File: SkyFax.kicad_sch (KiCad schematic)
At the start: 16 parts, among them J1 RJ11/12, J4 Conn_02x08_Odd_Even, J5 Conn_01x02, J6 Conn_01x02

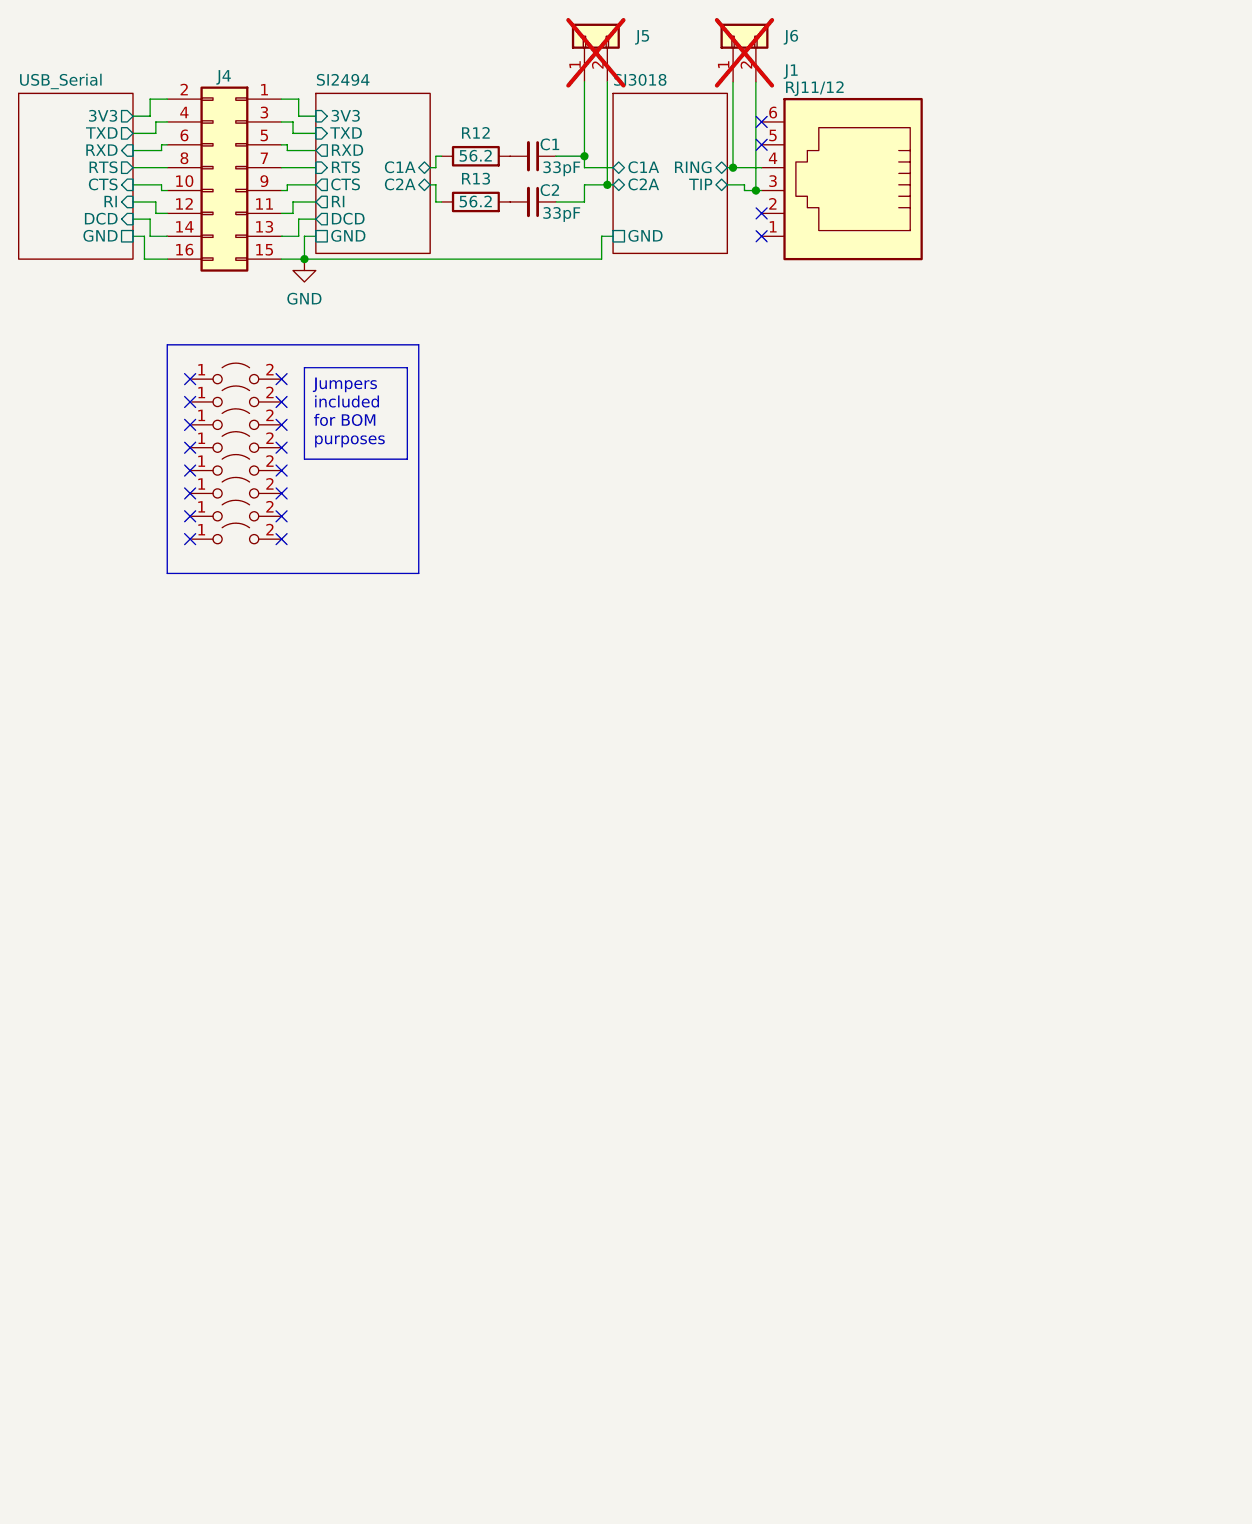
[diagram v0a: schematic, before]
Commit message: [4.0] M.2 Module. Sent to fab
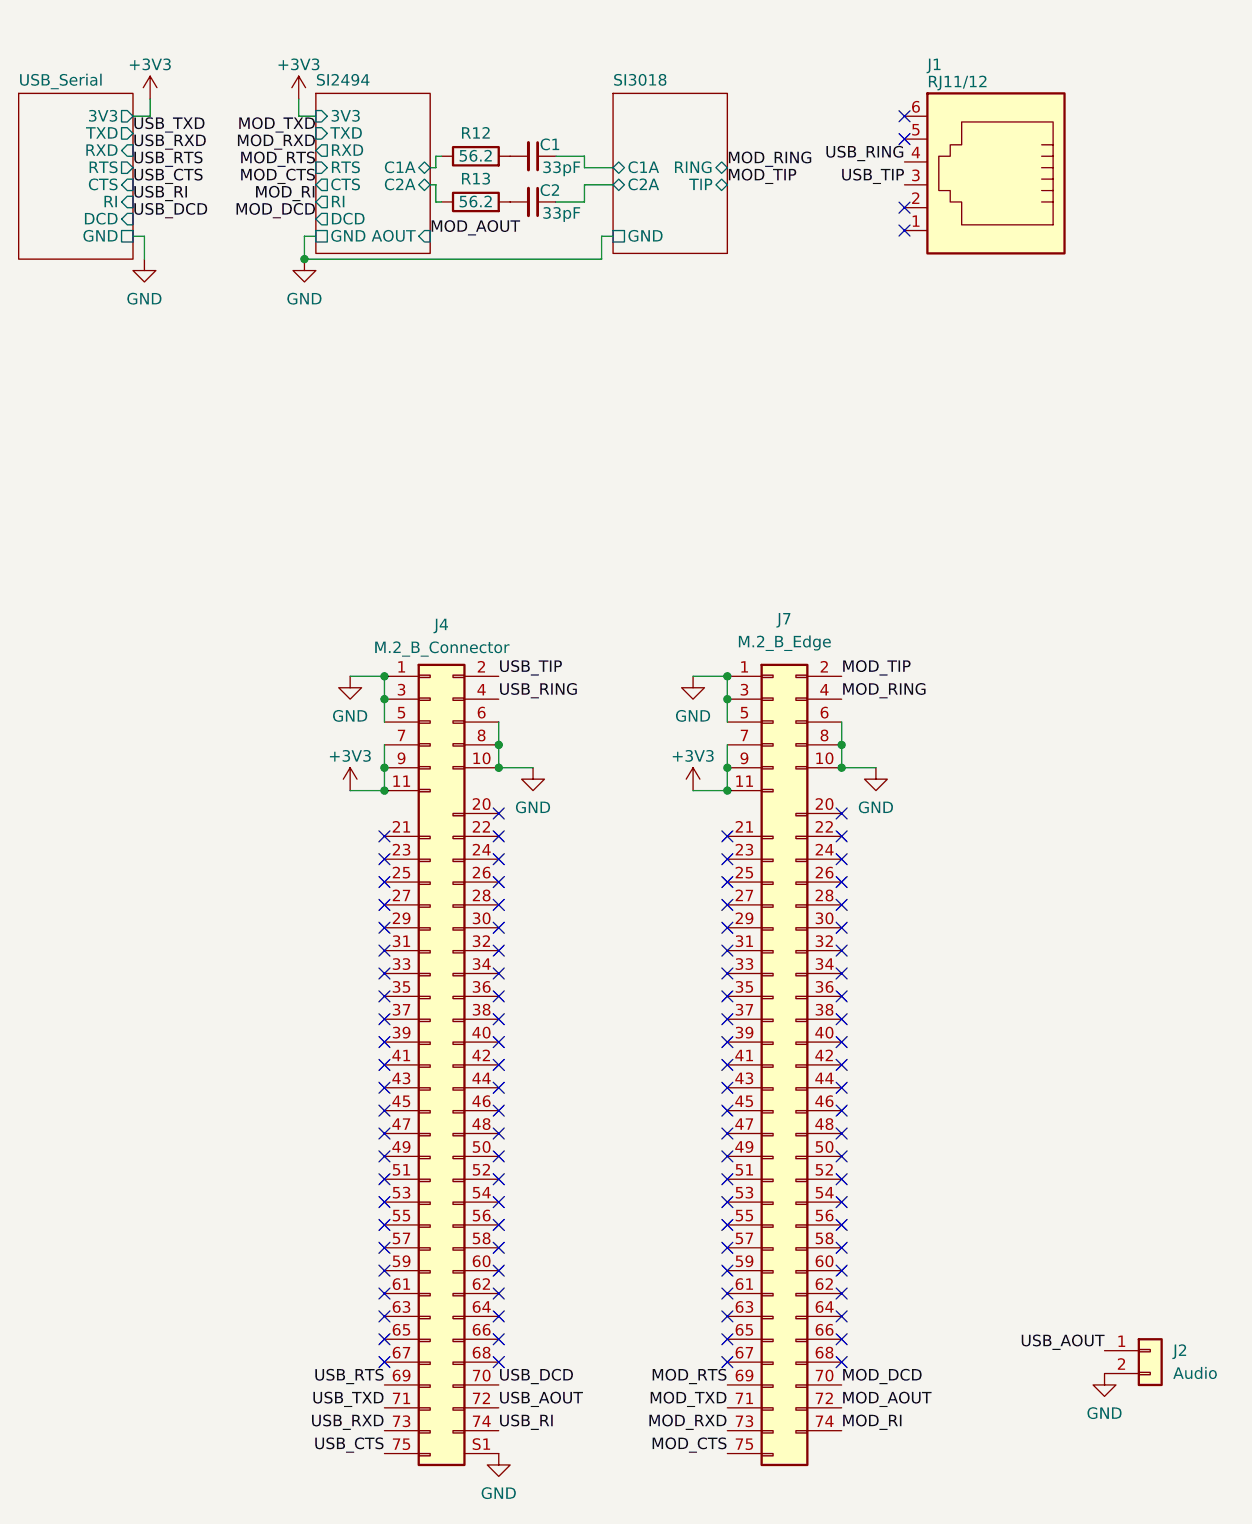
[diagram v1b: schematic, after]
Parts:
- removed J4: Conn_02x08_Odd_Even, Connector_PinHeader_2.54mm:PinHeader_2x08_P2.54mm_Vertical, symbol Connector_Generic:Conn_02x08_Odd_Even
- removed J5, J6: Conn_01x02, Connector_PinSocket_2.54mm:PinSocket_1x02_P2.54mm_Vertical, symbol Connector_Generic:Conn_01x02
- removed JP1, JP2, JP3, JP4, JP5, JP6, JP7, JP8: Jumper_2_Open, symbol Jumper:Jumper_2_Open
- added J2: Audio, Connector_PinSocket_2.54mm:PinSocket_1x02_P2.54mm_Vertical, symbol Connector_Generic:Conn_01x02
- added J4: M.2_B_Connector, SkyFax:AMPHENOL_MDT420B01001_2260, symbol SkyFax:M.2_B_Connector
- added J7: M.2_B_Edge, SkyFax:M.2-B-KEY_2260, symbol SkyFax:M.2_B_Edge
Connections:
- net GND: now also J2.2 (Pin_2), J4.1 (Pin_1), J4.10 (Pin_10), J4.3 (Pin_3), J4.5 (Pin_5), J4.6 (Pin_6), J4.8 (Pin_8), J4.S1 (SHIELD), J4.S2 (SHIELD), J7.1 (Pin_1), J7.10 (Pin_10), J7.3 (Pin_3), J7.5 (Pin_5), J7.6 (Pin_6), J7.8 (Pin_8)
- net SI3018/RING renamed USB_RING
- net USB_RING: now also J4.4 (Pin_4)
- net SI3018/TIP renamed USB_TIP
- net USB_TIP: now also J4.2 (Pin_2)
- new net +3V3: J4.11 (Pin_11), J4.7 (Pin_7), J4.9 (Pin_9), J7.11 (Pin_11), J7.7 (Pin_7), J7.9 (Pin_9)
- new net MOD_AOUT: J7.72 (Pin_72)
- new net MOD_CTS: J7.75 (Pin_75)
- new net MOD_DCD: J7.70 (Pin_70)
- new net MOD_RI: J7.74 (Pin_74)
- new net MOD_RING: J7.4 (Pin_4)
- new net MOD_RTS: J7.69 (Pin_69)
- new net MOD_RXD: J7.73 (Pin_73)
- new net MOD_TIP: J7.2 (Pin_2)
- new net MOD_TXD: J7.71 (Pin_71)
- new net USB_AOUT: J2.1 (Pin_1), J4.72 (Pin_72)
- new net USB_CTS: J4.75 (Pin_75)
- new net USB_DCD: J4.70 (Pin_70)
- new net USB_RI: J4.74 (Pin_74)
- new net USB_RTS: J4.69 (Pin_69)
- new net USB_RXD: J4.73 (Pin_73)
- new net USB_TXD: J4.71 (Pin_71)
- no-connect marks 20 -> 102
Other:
- sheet SI2494 ports: added AOUT; removed none
- moved on the sheet: J1

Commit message: [4.2] Sound card
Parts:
- J2: footprint Connector_PinSocket_2.54mm:PinSocket_1x02_P2.54mm_Vertical -> Connector_PinSocket_2.54mm:PinSocket_1x03_P2.54mm_Vertical; symbol Connector_Generic:Conn_01x02 -> Connector_Generic:Conn_01x03
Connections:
- net +3V3: now also J2.3 (Pin_3)
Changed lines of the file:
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@@
     (title "SkyFax")
     (date "2023-09-12")
-    (rev "4.0")
+    (rev "4.1")
     (company "Brian Hong")
     (comment 1 "@im_eningeer")
@@
     (stroke (width 0) (type default))
   )
+  (wire (pts (xy 139.7 173.99) (xy 137.795 173.99))
+    (stroke (width 0) (type default))
+  )
   (wire (pts (xy 59.69 96.52) (xy 55.88 96.52))
     (stroke (width 0) (type default))
@@
     (stroke (width 0) (type default))
   )
+  (wire (pts (xy 137.795 173.99) (xy 137.795 178.435))
+    (stroke (width 0) (type default))
+  )
   (wire (pts (xy 65.405 40.005) (xy 65.405 38.735))
     (stroke (width 0) (type default))
@@
   )
   (wire (pts (xy 110.49 101.6) (xy 110.49 104.14))
+    (stroke (width 0) (type default))
+  )
+  (wire (pts (xy 139.7 176.53) (xy 129.54 176.53))
+    (stroke (width 0) (type default))
+  )
+  (wire (pts (xy 129.54 168.91) (xy 129.54 176.53))
     (stroke (width 0) (type default))
   )
@@
     )
   )
-  (symbol (lib_id "power:GND") (at 139.7 173.99 0) (mirror y) (unit 1)
+  (symbol (lib_id "power:GND") (at 137.795 178.435 0) (mirror y) (unit 1)
     (in_bom yes) (on_board yes) (dnp no) (fields_autoplaced)
-    (property "Reference" "#PWR045" (at 139.7 180.34 0)
-      (effects (font (size 1.27 1.27)) hide)
-    )
-    (property "Value" "GND" (at 139.7 178.435 0)
-      (effects (font (size 1.27 1.27)))
-    )
-    (property "Footprint" "" (at 139.7 173.99 0)
-      (effects (font (size 1.27 1.27)) hide)
-    )
-    (property "Datasheet" "" (at 139.7 173.99 0)
+    (property "Reference" "#PWR045" (at 137.795 184.785 0)
+      (effects (font (size 1.27 1.27)) hide)
+    )
+    (property "Value" "GND" (at 137.795 182.88 0)
+      (effects (font (size 1.27 1.27)))
+    )
+    (property "Footprint" "" (at 137.795 178.435 0)
+      (effects (font (size 1.27 1.27)) hide)
+    )
+    (property "Datasheet" "" (at 137.795 178.435 0)
       (effects (font (size 1.27 1.27)) hide)
     )
@@
     )
   )
+  (symbol (lib_id "power:+3V3") (at 129.54 168.91 0) (unit 1)
+    (in_bom yes) (on_board yes) (dnp no)
+    (property "Reference" "#PWR046" (at 129.54 172.72 0)
+      (effects (font (size 1.27 1.27)) hide)
+    )
+    (property "Value" "+3V3" (at 129.54 165.1 0)
+      (effects (font (size 1.27 1.27)))
+    )
+    (property "Footprint" "" (at 129.54 168.91 0)
+      (effects (font (size 1.27 1.27)) hide)
+    )
+    (property "Datasheet" "" (at 129.54 168.91 0)
+      (effects (font (size 1.27 1.27)) hide)
+    )
+    (pin "1")
+    (instances
+      (project "SkyFax"
+        (path "/8648f108-1e45-4954-a197-b251f5522881"
+          (reference "#PWR046") (unit 1)
+        )
+        (path "/8648f108-1e45-4954-a197-b251f5522881/a903dc45-63a8-4bd9-abb6-8c8172debdba"
+          (reference "#PWR010") (unit 1)
+        )
+      )
+    )
+  )
   (symbol (lib_id "Device:R") (at 69.85 38.735 90) (unit 1)
     (in_bom yes) (on_board yes) (dnp no)
@@
     )
   )
-  (symbol (lib_id "Connector_Generic:Conn_01x02") (at 144.78 171.45 0) (unit 1)
+  (symbol (lib_id "Connector_Generic:Conn_01x03") (at 144.78 173.99 0) (unit 1)
     (in_bom yes) (on_board yes) (dnp no) (fields_autoplaced)
-    (property "Reference" "J2" (at 147.32 171.45 0)
+    (property "Reference" "J2" (at 147.32 173.99 0)
       (effects (font (size 1.27 1.27)) (justify left))
     )
-    (property "Value" "Audio" (at 147.32 173.99 0)
+    (property "Value" "Audio" (at 147.32 176.53 0)
       (effects (font (size 1.27 1.27)) (justify left))
     )
-    (property "Footprint" "Connector_PinSocket_2.54mm:PinSocket_1x02_P2.54mm_Vertical" (at 144.78 171.45 0)
-      (effects (font (size 1.27 1.27)) hide)
-    )
-    (property "Datasheet" "~" (at 144.78 171.45 0)
+    (property "Footprint" "Connector_PinSocket_2.54mm:PinSocket_1x03_P2.54mm_Vertical" (at 144.78 173.99 0)
+      (effects (font (size 1.27 1.27)) hide)
+    )
+    (property "Datasheet" "~" (at 144.78 173.99 0)
       (effects (font (size 1.27 1.27)) hide)
     )
     (pin "1")
     (pin "2")
-    (instances
-      (project "SkyFax"
+    (pin "3")
+    (instances
+      (project "SkyFax"
